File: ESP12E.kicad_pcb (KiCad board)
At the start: 2 copper layers, 100 x 100 mm, 96 parts, among them J10 Sol_1, J3 UART, J4 12v PWR, J5 Battery, J6 Sol_2, J7 Sol_3, J8 Sol_4, J9 Motor, Q1 RU3560L, Q2 IRF540N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

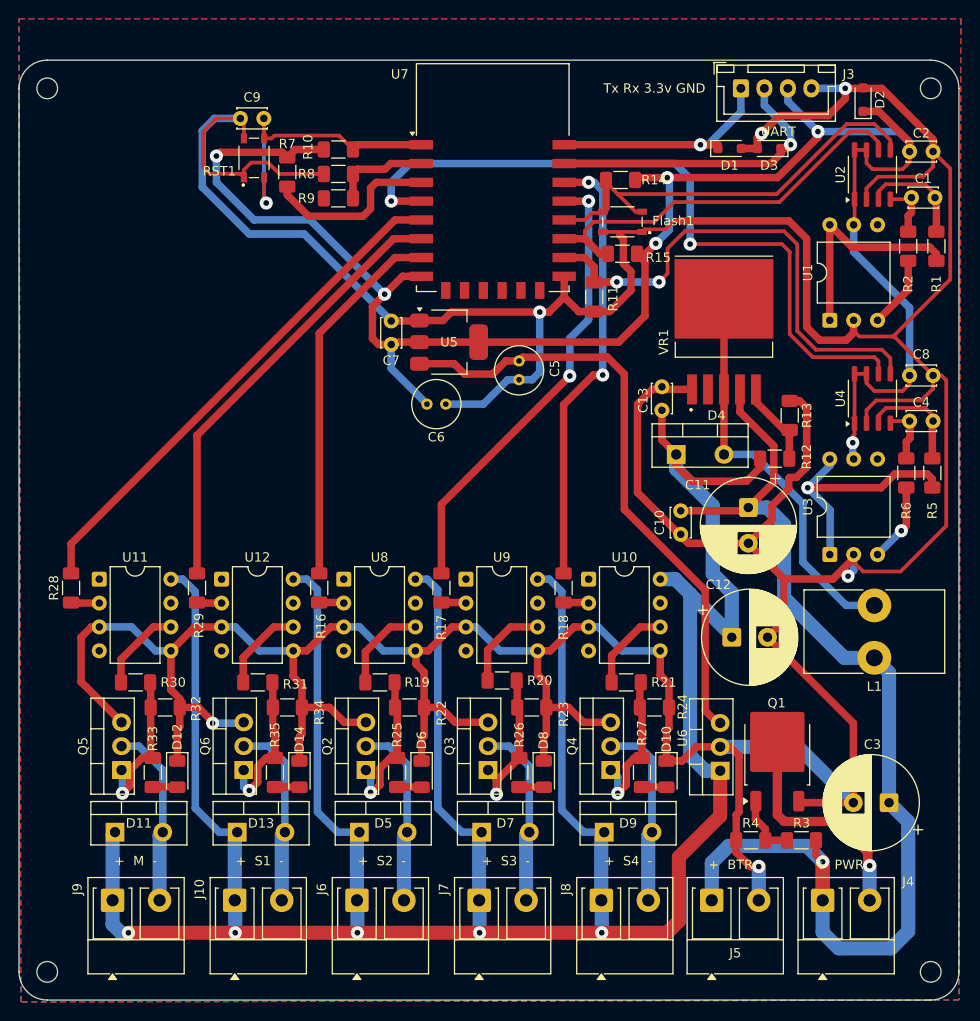
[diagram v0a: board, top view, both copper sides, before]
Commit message: Feat: the board now has a circuit that manage       the switch between Battery and Adaptor Power.
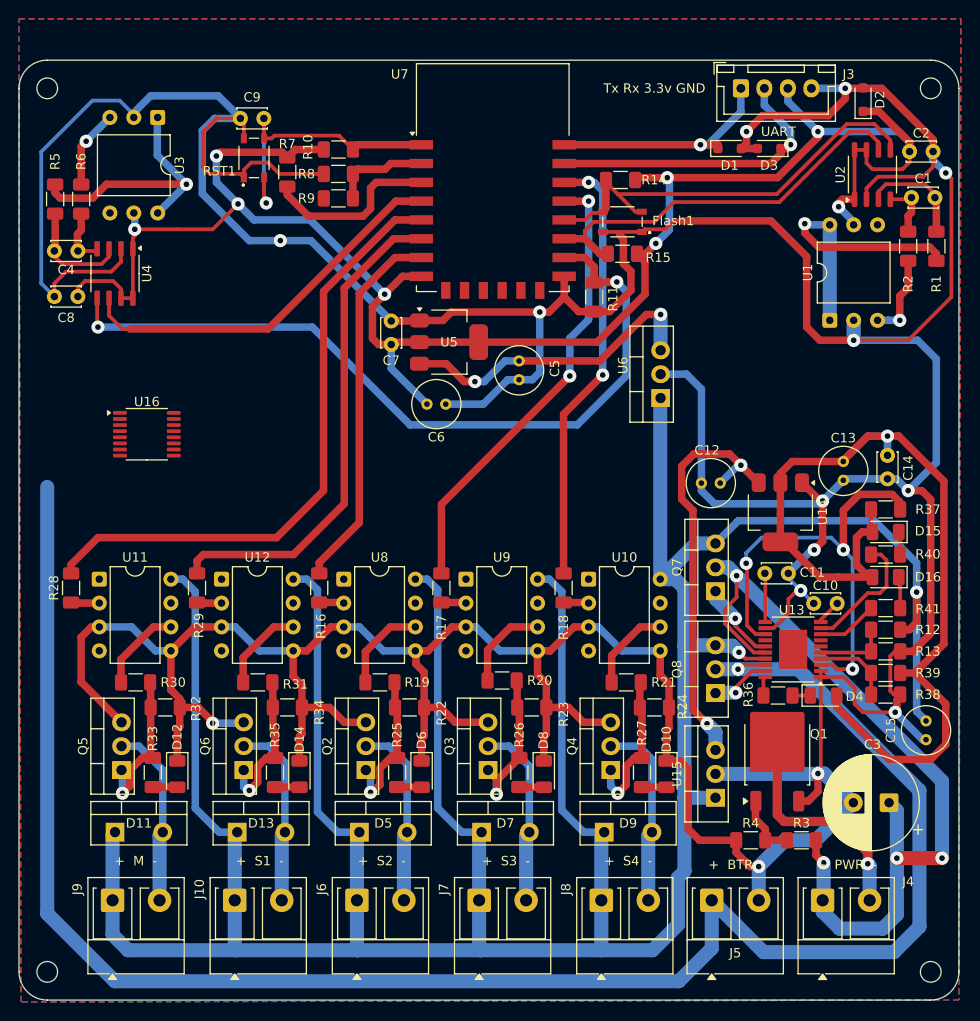
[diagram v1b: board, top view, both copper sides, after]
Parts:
- removed L1: 47uH, Inductor_THT:L_Toroid_Vertical_L14.7mm_W8.6mm_P5.58mm_Pulse_KM-1
- removed VR1: XL6019E1, Converter_DCDC:TO-263-5
- added C14: 100uF, Capacitor_THT:C_Disc_D3.0mm_W2.0mm_P2.50mm, F.Cu at (117.4, 64.5)
- added C15: 10uF, Capacitor_THT:C_Radial_D5.0mm_H5.0mm_P2.00mm, F.Cu at (121.5, 92.3)
- added D15: LED, LED_SMD:LED_1206_3216Metric, F.Cu at (117.2, 70.2)
- added D16: LED, LED_SMD:LED_1206_3216Metric, F.Cu at (117.2, 75.0)
- added Q7: 2SJ174, Package_TO_SOT_THT:TO-220-3_Vertical, F.Cu at (99.1, 76.5)
- added Q8: 2SJ174, Package_TO_SOT_THT:TO-220-3_Vertical, F.Cu at (99.1, 87.3)
- added R36: 1k, Resistor_SMD:R_1206_3216Metric_Pad1.30x1.75mm_HandSolder, F.Cu at (105.8, 87.6)
- added R37: 10k, Resistor_SMD:R_1206_3216Metric_Pad1.30x1.75mm_HandSolder, F.Cu at (117.2, 67.8)
- added R38: 100k, Resistor_SMD:R_1206_3216Metric_Pad1.30x1.75mm_HandSolder, F.Cu at (117.2, 87.5)
- added R39: 511k, Resistor_SMD:R_1206_3216Metric_Pad1.30x1.75mm_HandSolder, F.Cu at (117.2, 85.2)
- added R40: 1k, Resistor_SMD:R_1206_3216Metric_Pad1.30x1.75mm_HandSolder, F.Cu at (117.2, 72.6)
- added R41: 1k, Resistor_SMD:R_1206_3216Metric_Pad1.30x1.75mm_HandSolder, F.Cu at (117.2, 78.3)
- added U13: LTC2952, Package_SO:ETSSOP-20-1EP_4.4x6.5mm_P0.65mm_EP3x4.2mm, F.Cu at (107.3, 82.7)
- added U14: AMS1117-3.3, Package_TO_SOT_SMD:SOT-223-3_TabPin2, F.Cu at (106.0, 68.1)
- added U15: LM7805_TO220, Package_TO_SOT_THT:TO-220-3_Vertical, F.Cu at (99.1, 98.5)
- added U16: CN3703, Package_SO:TSSOP-16_4.4x5mm_P0.65mm, F.Cu at (38.6, 59.8)
- C10: value 100nF -> 22nF
- C11: value 220uF/16V -> 68nF; footprint Capacitor_THT:CP_Radial_D10.0mm_P3.80mm -> Capacitor_THT:C_Disc_D3.0mm_W2.0mm_P2.50mm
- C12: value 220uF/16V -> 10uF; footprint Capacitor_THT:CP_Radial_D10.0mm_P3.80mm -> Capacitor_THT:C_Radial_D5.0mm_H5.0mm_P2.00mm
- C13: value 100nF -> 10uF; footprint Capacitor_THT:C_Disc_D3.0mm_W2.0mm_P2.50mm -> Capacitor_THT:C_Radial_D5.0mm_H5.0mm_P2.00mm
- D4: value MBR745 -> LED; footprint Package_TO_SOT_THT:TO-220-2_Vertical -> LED_SMD:LED_1206_3216Metric
- R12: value 30k -> 1.3M
- R13: value 3k3 -> 100k
- moved R5 97.8 mm to (28.8, 34.8), turned to 90 degrees
- moved C4 95.2 mm to (28.8, 40.3), turned to 0 degrees
- moved R6 92.5 mm to (31.6, 34.8), turned to 90 degrees
- moved C8 88.9 mm to (31.3, 45.1), turned to 180 degrees
- moved U3 85.3 mm to (39.8, 26.1), turned to -90 degrees
- moved U4 81.7 mm to (35.2, 42.7), turned to -90 degrees
- moved U6 40.2 mm to (93.3, 56.0)
- moved D4 30.1 mm to (110.6, 87.6)
- moved R13 27.1 mm to (117.2, 82.9), turned to 180 degrees
- moved C13 21.7 mm to (112.7, 64.7), turned to 90 degrees
- moved R12 21.7 mm to (117.2, 80.6)
- moved C12 16.7 mm to (97.6, 65.0)
- moved C10 15.9 mm to (109.5, 77.8), turned to 0 degrees
- moved C11 8.19 mm to (106.8, 74.6), turned to 180 degrees
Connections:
- C10 pad 2: V_btr -> Net-(U13-ONT)
- C11 pad 1: V_btr -> GND
- C11 pad 2: GND -> Net-(U13-OFFT)
- C12 pad 1: +12V -> GND
- C12 pad 2: GND -> Net-(U14-VI)
- C13 pad 2: +12V -> +3.3VP
- C3 pad 1: V_btr -> PWR_{in}
- D11 pad 1: +12V -> PWR_{out}
- D13 pad 1: +12V -> PWR_{out}
- D4 pad 1: +12V -> Net-(D4-K)
- D4 pad 2: Net-(D4-A) -> +3.3VP
- D5 pad 1: +12V -> PWR_{out}
- D7 pad 1: +12V -> PWR_{out}
- D9 pad 1: +12V -> PWR_{out}
- J10 pad 1: +12V -> PWR_{out}
- J4 pad 1: V_btr -> PWR_{in}
- J6 pad 1: +12V -> PWR_{out}
- J7 pad 1: +12V -> PWR_{out}
- J8 pad 1: +12V -> PWR_{out}
- J9 pad 1: +12V -> PWR_{out}
- R12 pad 1: Net-(VR1-FB) -> PWR_{out}
- R12 pad 2: +12V -> Net-(U13-PFI)
- R13 pad 2: Net-(VR1-FB) -> Net-(U13-PFI)
- R3 pad 2: V_btr -> PWR_{in}
- U10 pad 8: +12V -> PWR_{out}
- U11 pad 8: +12V -> PWR_{out}
- U12 pad 8: +12V -> PWR_{out}
- U6 pad 1: +12V -> PWR_{out}
- U8 pad 8: +12V -> PWR_{out}
- U9 pad 8: +12V -> PWR_{out}
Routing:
- net PWR_{out}: track 0.00 -> 377.6 mm, vias 0 -> 2
- net +12V: track 334.3 -> 0.00 mm, vias 5 -> 0
- net +3.3VP: track 0.00 -> 105.1 mm, vias 0 -> 1
- net PWR_{in}: track 0.00 -> 87.2 mm, vias 0 -> 4
- net V_btr: track 119.7 -> 195.8 mm
- net GND: track 591.1 -> 661.0 mm, vias 6 -> 14
- net Net-(U13-~{INT}): track 0.00 -> 50.4 mm, vias 0 -> 3
- net Net-(U14-VI): track 0.00 -> 44.8 mm, vias 0 -> 2
- net Net-(D4-A): track 42.8 -> 0.00 mm
- net D0/GPIO16: track 77.1 -> 41.3 mm, vias 2 -> 0
- net +5V: track 65.3 -> 33.2 mm, vias 0 -> 2
- net D8/GPIO15/SS: track 53.2 -> 83.9 mm
- net Net-(U13-~{PFO}): track 0.00 -> 13.4 mm
- net D5/GPIO14/SCLK: track 54.7 -> 65.8 mm
- net Net-(VR1-FB): track 8.88 -> 0.00 mm
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
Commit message: feat: Battery charging Circuit is added.
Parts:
- added C16: 10uF, Capacitor_THT:C_Radial_D5.0mm_H5.0mm_P2.00mm, F.Cu at (55.3, 67.5)
- added C17: 10uF, Capacitor_THT:C_Radial_D5.0mm_H5.0mm_P2.00mm, F.Cu at (39.6, 57.5)
- added C18: 100nF, Capacitor_THT:C_Disc_D3.0mm_W2.0mm_P2.50mm, F.Cu at (48.6, 66.3)
- added C19: 220nF, Capacitor_THT:C_Disc_D3.0mm_W2.0mm_P2.50mm, F.Cu at (35.4, 67.9)
- added C20: 470pF, Capacitor_THT:C_Disc_D3.0mm_W2.0mm_P2.50mm, F.Cu at (29.4, 65.6)
- added C21: 10uF, Capacitor_THT:C_Radial_D5.0mm_H5.0mm_P2.00mm, F.Cu at (29.0, 69.3)
- added D17: LED, LED_SMD:LED_1206_3216Metric, F.Cu at (30.6, 57.1)
- added D18: LED, LED_SMD:LED_1206_3216Metric, F.Cu at (30.6, 54.6)
- added D19: SS36, Diode_SMD:D_SMA, F.Cu at (41.1, 47.8)
- added D20: SS36, Diode_SMD:D_SMA, F.Cu at (37.0, 51.5)
- added L1: 22uH, Inductor_SMD:L_12x12mm_H4.5mm, F.Cu at (49.9, 45.9)
- added L2: 22uH, Inductor_SMD:L_12x12mm_H4.5mm, F.Cu at (77.6, 63.0)
- added Q9: 2SJ174, Package_TO_SOT_THT:TO-220-3_Vertical, F.Cu at (48.8, 57.2)
- added R42: 1k, Resistor_SMD:R_1206_3216Metric_Pad1.30x1.75mm_HandSolder, F.Cu at (30.7, 52.1)
- added R43: 1k, Resistor_SMD:R_1206_3216Metric_Pad1.30x1.75mm_HandSolder, F.Cu at (30.6, 49.6)
- added R44: 10k, Resistor_SMD:R_1206_3216Metric_Pad1.30x1.75mm_HandSolder, F.Cu at (31.8, 60.9)
- added R45: 10k, Resistor_SMD:R_1206_3216Metric_Pad1.30x1.75mm_HandSolder, F.Cu at (29.5, 61.8)
- added R46: 120, Resistor_SMD:R_1206_3216Metric_Pad1.30x1.75mm_HandSolder, F.Cu at (41.6, 67.9)
- added R47: 0.1, Resistor_SMD:R_2512_6332Metric_Pad1.40x3.35mm_HandSolder, F.Cu at (63.7, 64.1)
- moved C6 28.0 mm to (95.4, 43.9), turned to 90 degrees
- moved C5 4.00 mm to (78.4, 50.0), turned to -90 degrees
- moved U16 3.96 mm to (40.4, 63.3)
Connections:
- U16 pad 1: unconnected-(U16-VG-Pad1) -> Net-(U16-VG)
- U16 pad 10: unconnected-(U16-test-Pad10) -> GND
- U16 pad 11: unconnected-(U16-COM3-Pad11) -> Net-(U16-COM3)
- U16 pad 13: unconnected-(U16-CSP-Pad13) -> PWR_{out}
- U16 pad 15: unconnected-(U16-VCC-Pad15) -> PWR_{out}
- U16 pad 16: unconnected-(U16-DRV-Pad16) -> Net-(Q9-G)
- U16 pad 2: unconnected-(U16-PGND-Pad2) -> GND
- U16 pad 3: unconnected-(U16-GND-Pad3) -> GND
- U16 pad 4: unconnected-(U16-~{CHRG}-Pad4) -> Net-(D18-K)
- U16 pad 5: unconnected-(U16-~{DONE}-Pad5) -> Net-(D17-K)
- U16 pad 6: unconnected-(U16-TEMP-Pad6) -> Net-(U16-TEMP)
- U16 pad 7: unconnected-(U16-EOC-Pad7) -> Net-(U16-EOC)
- U16 pad 8: unconnected-(U16-COM1-Pad8) -> Net-(U16-COM1)
- U16 pad 9: unconnected-(U16-COM2-Pad9) -> Net-(U16-COM2)
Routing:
- net PWR_{out}: track 377.6 -> 499.5 mm, vias 2 -> 6
- net GND: track 661.0 -> 754.0 mm, vias 14 -> 17
- net Net-(D19-K): track 0.00 -> 51.6 mm, vias 0 -> 2
- net V_btr: track 195.8 -> 229.5 mm, vias 1 -> 2
- net Net-(D19-A): track 0.00 -> 23.2 mm, vias 0 -> 1
- net Net-(D18-K): track 0.00 -> 12.4 mm
- net Net-(D17-K): track 0.00 -> 10.9 mm
- net D8/GPIO15/SS: track 83.9 -> 93.0 mm
- net Net-(U16-EOC): track 0.00 -> 8.72 mm
- net Net-(U16-COM3): track 0.00 -> 8.63 mm
- net Net-(D18-A): track 0.00 -> 7.65 mm
- net Net-(Q9-G): track 0.00 -> 7.11 mm
- net D2/SDA/GPIO4: track 48.7 -> 55.5 mm
- net Net-(D17-A): track 0.00 -> 6.73 mm
- net Net-(U16-TEMP): track 0.00 -> 6.53 mm
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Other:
- board text added: "~{CHRG}"
- board text added: "~{DONE}"
